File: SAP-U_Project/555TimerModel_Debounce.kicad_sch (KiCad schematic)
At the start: 13 parts, among them Q2 BC107, U10 Inverter, U4 Comparator 2, U5 SR LATCH

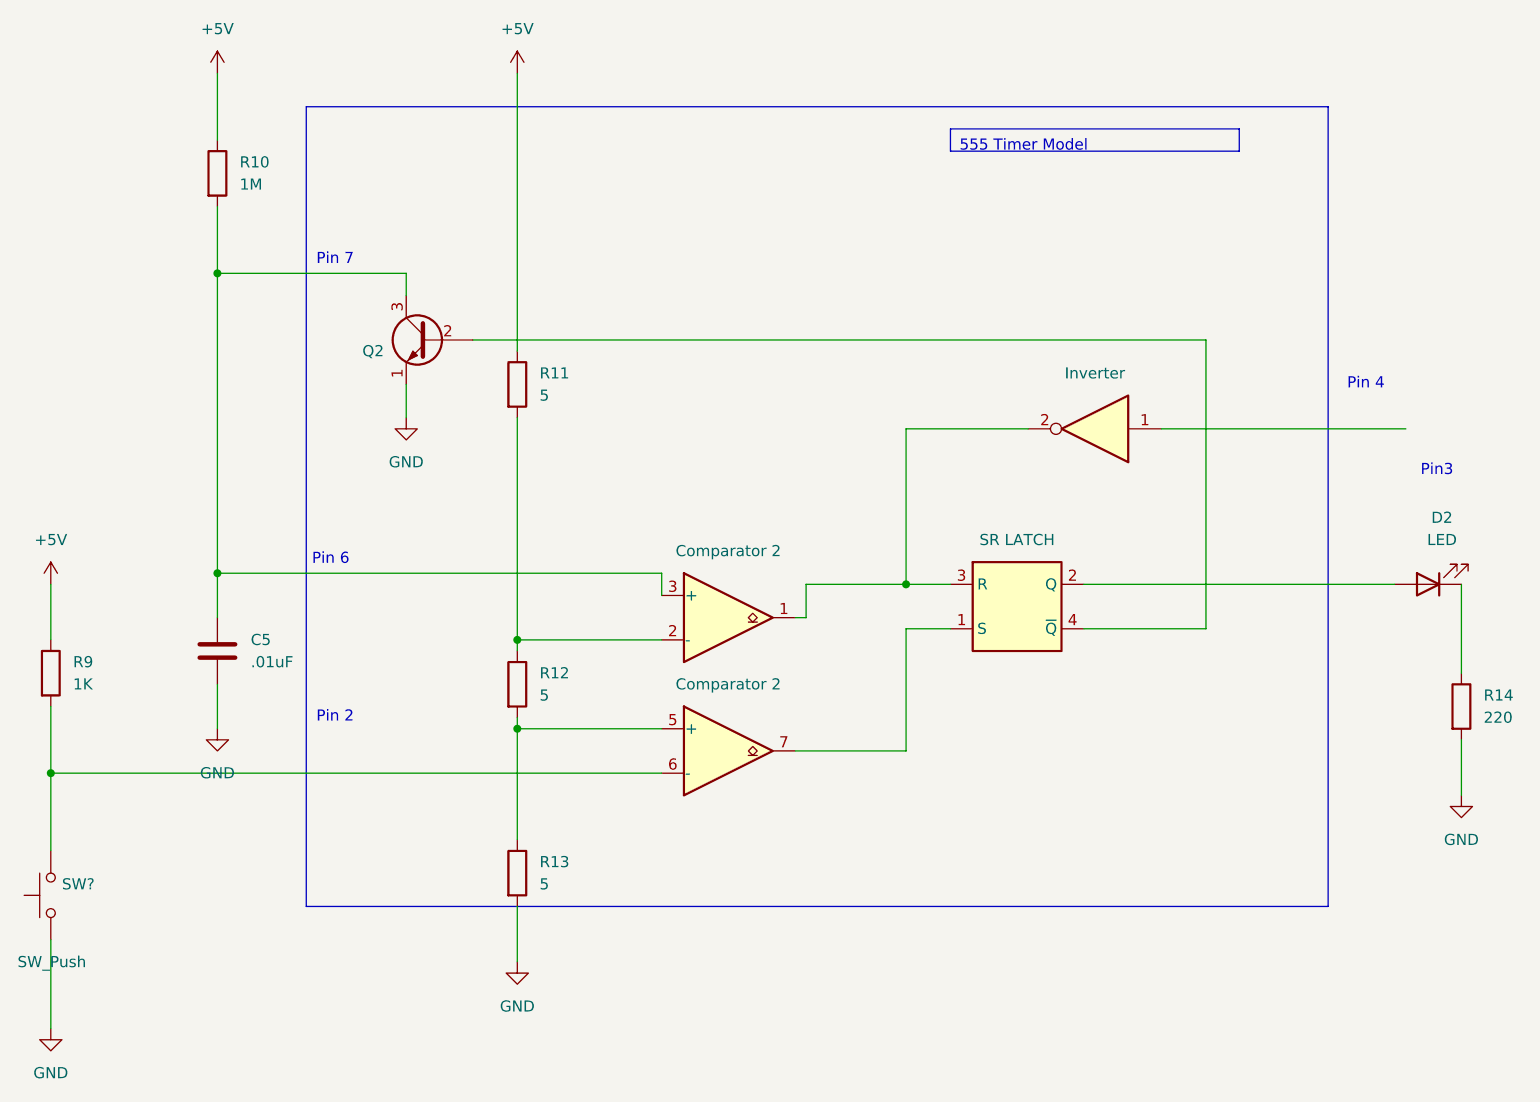
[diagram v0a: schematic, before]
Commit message: Checkpoint: added switching logic
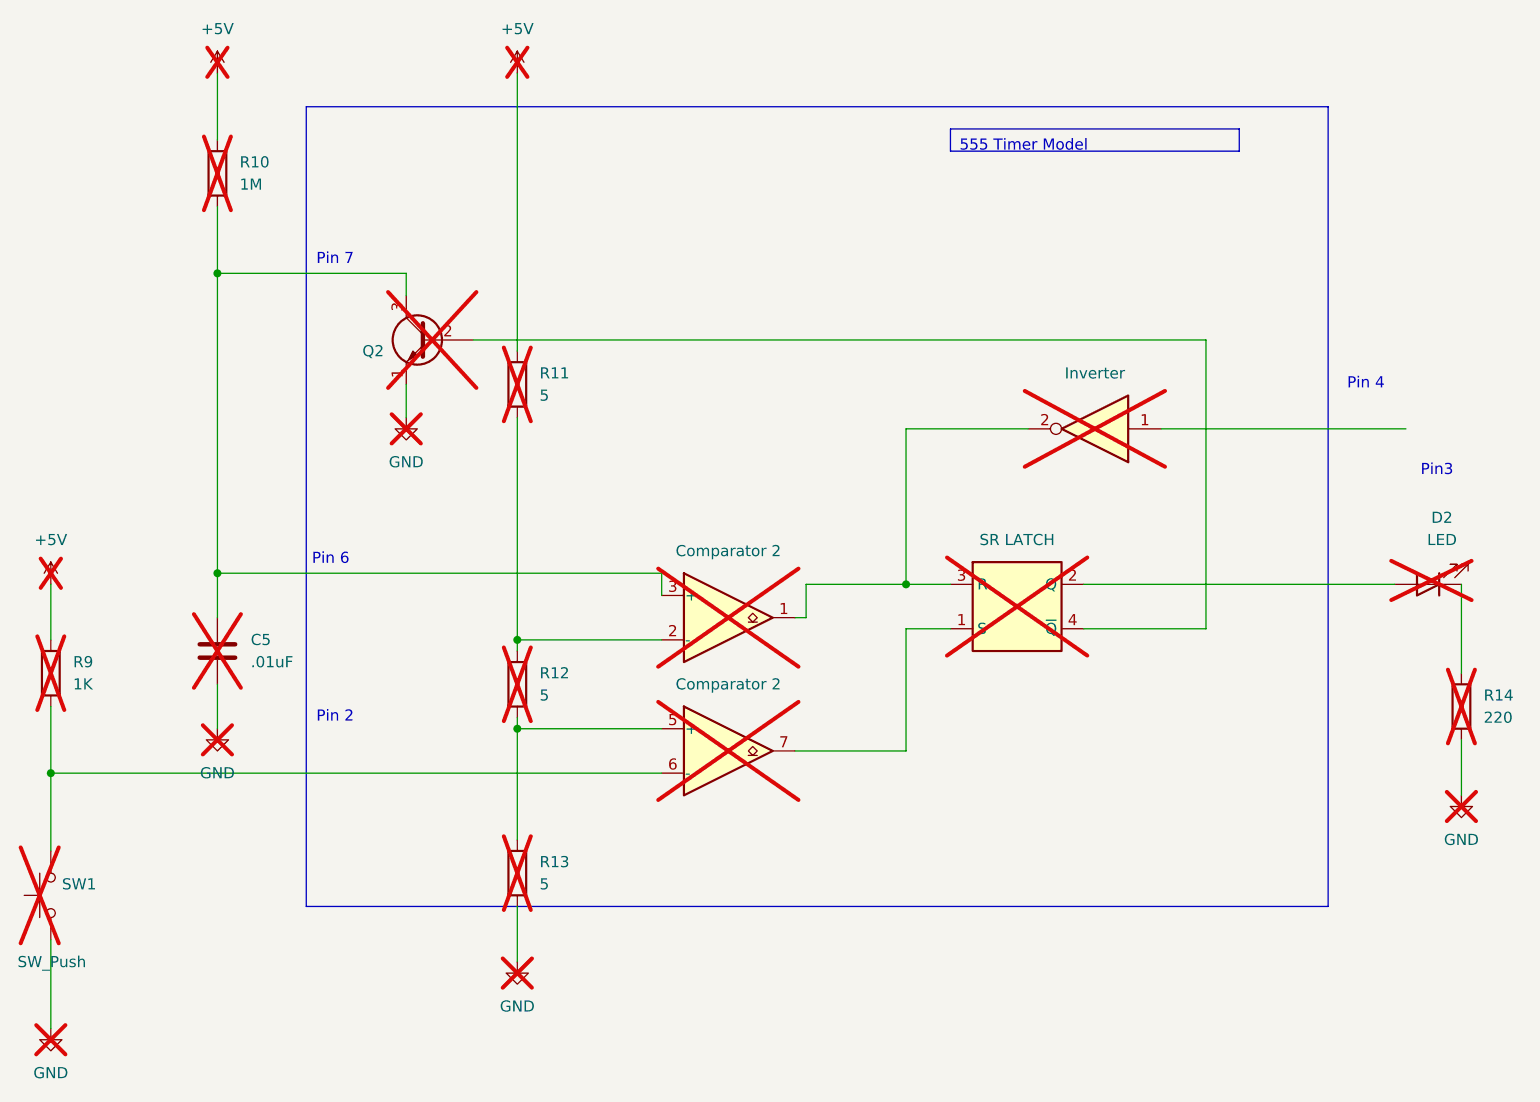
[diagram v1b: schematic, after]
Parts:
- C5, D2, Q2, R10, R11, R12, R13, R14, R9, U10, U4, U5: now not fitted; now left out of the parts list
- SW1: renamed from SW?; now not fitted; now left out of the parts list
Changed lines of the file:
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@@
 		(unit 1)
 		(exclude_from_sim yes)
-		(in_bom yes)
-		(on_board yes)
-		(dnp no)
+		(in_bom no)
+		(on_board no)
+		(dnp yes)
 		(fields_autoplaced yes)
 		(property "Reference" "#PWR011"
@@
 		(unit 1)
 		(exclude_from_sim yes)
-		(in_bom yes)
-		(on_board yes)
-		(dnp no)
+		(in_bom no)
+		(on_board no)
+		(dnp yes)
 		(fields_autoplaced yes)
 		(property "Reference" "R9"
@@
 		(unit 1)
 		(exclude_from_sim yes)
-		(in_bom yes)
-		(on_board yes)
-		(dnp no)
+		(in_bom no)
+		(on_board no)
+		(dnp yes)
 		(fields_autoplaced yes)
 		(property "Reference" "R12"
@@
 		(unit 2)
 		(exclude_from_sim yes)
-		(in_bom yes)
-		(on_board yes)
-		(dnp no)
+		(in_bom no)
+		(on_board no)
+		(dnp yes)
 		(fields_autoplaced yes)
 		(property "Reference" "U4"
@@
 		(at 153.67 78.74 180)
 		(unit 1)
-		(exclude_from_sim no)
-		(in_bom yes)
-		(on_board yes)
-		(dnp no)
+		(exclude_from_sim yes)
+		(in_bom no)
+		(on_board no)
+		(dnp yes)
 		(fields_autoplaced yes)
 		(property "Reference" "U10"
@@
 		(unit 1)
 		(exclude_from_sim yes)
-		(in_bom yes)
-		(on_board yes)
-		(dnp no)
+		(in_bom no)
+		(on_board no)
+		(dnp yes)
 		(fields_autoplaced yes)
 		(property "Reference" "C5"
@@
 		(unit 1)
 		(exclude_from_sim yes)
-		(in_bom yes)
-		(on_board yes)
-		(dnp no)
+		(in_bom no)
+		(on_board no)
+		(dnp yes)
 		(fields_autoplaced yes)
 		(property "Reference" "#PWR012"
@@
 		(unit 1)
 		(exclude_from_sim yes)
-		(in_bom yes)
-		(on_board yes)
-		(dnp no)
+		(in_bom no)
+		(on_board no)
+		(dnp yes)
 		(fields_autoplaced yes)
 		(property "Reference" "R11"
@@
 		(unit 1)
 		(exclude_from_sim yes)
-		(in_bom yes)
-		(on_board yes)
-		(dnp no)
+		(in_bom no)
+		(on_board no)
+		(dnp yes)
 		(fields_autoplaced yes)
 		(property "Reference" "R14"
@@
 		(unit 1)
 		(exclude_from_sim yes)
-		(in_bom yes)
-		(on_board yes)
-		(dnp no)
+		(in_bom no)
+		(on_board no)
+		(dnp yes)
 		(fields_autoplaced yes)
 		(property "Reference" "#PWR09"
@@
 		(unit 1)
 		(exclude_from_sim yes)
-		(in_bom yes)
-		(on_board yes)
-		(dnp no)
+		(in_bom no)
+		(on_board no)
+		(dnp yes)
 		(fields_autoplaced yes)
 		(property "Reference" "U4"
@@
 		(unit 1)
 		(exclude_from_sim yes)
-		(in_bom yes)
-		(on_board yes)
-		(dnp no)
+		(in_bom no)
+		(on_board no)
+		(dnp yes)
 		(fields_autoplaced yes)
 		(property "Reference" "#PWR014"
@@
 		(unit 1)
 		(exclude_from_sim yes)
-		(in_bom yes)
-		(on_board yes)
-		(dnp no)
+		(in_bom no)
+		(on_board no)
+		(dnp yes)
 		(fields_autoplaced yes)
 		(property "Reference" "R10"
@@
 		(unit 1)
 		(exclude_from_sim yes)
-		(in_bom yes)
-		(on_board yes)
-		(dnp no)
+		(in_bom no)
+		(on_board no)
+		(dnp yes)
 		(property "Reference" "Q2"
 			(at 72.39 69.8501 0)
@@
 		(unit 1)
 		(exclude_from_sim yes)
-		(in_bom yes)
-		(on_board yes)
-		(dnp no)
+		(in_bom no)
+		(on_board no)
+		(dnp yes)
 		(fields_autoplaced yes)
 		(property "Reference" "#PWR010"
@@
 		(unit 1)
 		(exclude_from_sim yes)
-		(in_bom yes)
-		(on_board yes)
-		(dnp no)
+		(in_bom no)
+		(on_board no)
+		(dnp yes)
 		(fields_autoplaced yes)
 		(property "Reference" "R13"
@@
 		(unit 1)
 		(exclude_from_sim yes)
-		(in_bom yes)
-		(on_board yes)
-		(dnp no)
+		(in_bom no)
+		(on_board no)
+		(dnp yes)
 		(fields_autoplaced yes)
 		(property "Reference" "U5"
@@
 		(unit 1)
 		(exclude_from_sim yes)
-		(in_bom yes)
-		(on_board yes)
-		(dnp no)
+		(in_bom no)
+		(on_board no)
+		(dnp yes)
 		(fields_autoplaced yes)
 		(property "Reference" "#PWR013"
@@
 		(unit 1)
 		(exclude_from_sim yes)
-		(in_bom yes)
-		(on_board yes)
-		(dnp no)
+		(in_bom no)
+		(on_board no)
+		(dnp yes)
 		(fields_autoplaced yes)
 		(property "Reference" "#PWR016"
@@
 		(at 34.29 132.08 90)
 		(unit 1)
-		(exclude_from_sim no)
-		(in_bom yes)
-		(on_board yes)
-		(dnp no)
-		(property "Reference" "SW?"
+		(exclude_from_sim yes)
+		(in_bom no)
+		(on_board no)
+		(dnp yes)
+		(property "Reference" "SW1"
 			(at 35.56 130.8099 90)
 			(effects
@@
 			(project "SAP-U_Project"
 				(path "/e63e39d7-6ac0-4ffd-8aa3-1841a4541b55/7f1b9d87-3d1d-4a5d-8055-cfab36c6883b/1215a834-8751-4afe-a39a-5cb85338559e"
-					(reference "SW?")
+					(reference "SW1")
 					(unit 1)
 				)
@@
 		(unit 1)
 		(exclude_from_sim yes)
-		(in_bom yes)
-		(on_board yes)
-		(dnp no)
+		(in_bom no)
+		(on_board no)
+		(dnp yes)
 		(fields_autoplaced yes)
 		(property "Reference" "D2"
@@
 		(unit 1)
 		(exclude_from_sim yes)
-		(in_bom yes)
-		(on_board yes)
-		(dnp no)
+		(in_bom no)
+		(on_board no)
+		(dnp yes)
 		(fields_autoplaced yes)
 		(property "Reference" "#PWR015"
